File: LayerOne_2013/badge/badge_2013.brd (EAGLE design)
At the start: 81.3 x 81.3 mm, 122 parts, among them CON2 EXT, CON6 J8, CON8 J3, IC4 TL064D, U1 UG-2864HSWEG01, U2 AP7333-33SOT23-3, U4 TPS60403, X2 NX3225GA

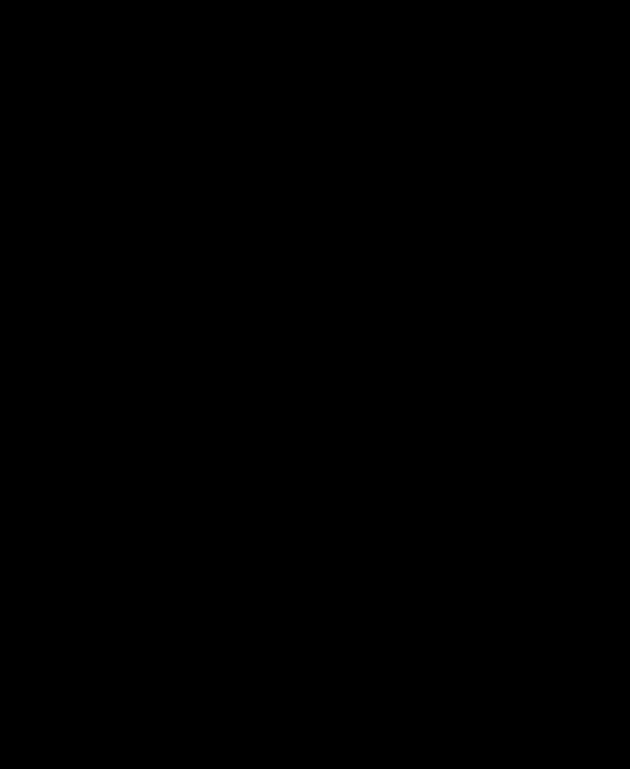
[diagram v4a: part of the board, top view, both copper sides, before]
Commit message: 
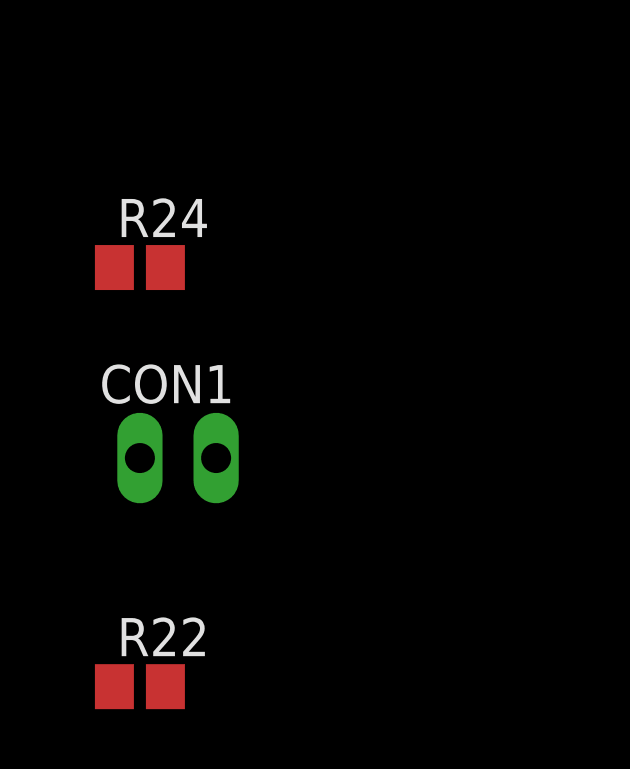
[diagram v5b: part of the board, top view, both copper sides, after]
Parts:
- added CON1: EXT, microbuilder:1X02_OVAL
- added R22: 180K, resistor:R0805
- added R24: 3K, resistor:R0805
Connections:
- removed net RESET: IC2.35
- removed net VBUS: Z1.4
- new net DAC: IC2.6, R22.2
- new net DAT: CON1.1, IC2.34
- new net N$38: CON1.2, IC2.35
- new net N$6: CON2.1, R24.1
- net +5V: now also Z1.4
- net D/C: now also IC2.7; no longer IC2.6
- net N$19: now also R24.2; no longer CON2.1
- net N$24: now also R22.1
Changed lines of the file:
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@@
 <element name="JP1" library="microbuilder" package="JUMPER3" value="" x="16.51" y="3.81"/>
 <element name="SJ1" library="microbuilder" package="SOLDERJUMPER_REFLOW_NOPASTE" value="" x="2.54" y="34.29"/>
+<element name="R24" library="resistor" package="R0805" value="3K" x="-59.69" y="-44.45"/>
+<element name="CON1" library="microbuilder" package="1X02_OVAL" value="EXT" x="-58.42" y="-50.8"/>
+<element name="R22" library="resistor" package="R0805" value="180K" x="-59.69" y="-58.42"/>
 </elements>
 <signals>
@@
 <signal name="N$19">
 <contactref element="IC2" pad="25"/>
-<contactref element="CON2" pad="1"/>
-<wire x1="13.97" y1="-13.97" x2="5.75" y2="-2.4" width="0" layer="19" extent="1-1"/>
+<contactref element="R24" pad="2"/>
+<wire x1="5.75" y1="-2.4" x2="-58.84" y2="-44.45" width="0" layer="19" extent="1-1"/>
 </signal>
 <signal name="+5V">
@@
 <contactref element="IC4" pad="4"/>
 <contactref element="JP6" pad="1"/>
+<contactref element="Z1" pad="4"/>
 <wire x1="-46.09" y1="-10.16" x2="-42.86" y2="-35.29" width="0" layer="19" extent="1-1"/>
 <wire x1="-55.88" y1="1.21" x2="-46.09" y2="-10.16" width="0" layer="19" extent="1-1"/>
@@
 <wire x1="-1.3" y1="13.255" x2="-17.41" y2="24.13" width="0" layer="19" extent="1-16"/>
 <wire x1="22.86" y1="19.05" x2="-1.3" y2="13.255" width="0" layer="19" extent="16-16"/>
-</signal>
-<signal name="VBUS">
-<contactref element="Z1" pad="4"/>
+<wire x1="24.4" y1="0.95" x2="22.86" y2="19.05" width="0" layer="19" extent="16-16"/>
 </signal>
 <signal name="D-">
@@
 <signal name="D/C">
 <contactref element="U1" pad="15"/>
-<contactref element="IC2" pad="6"/>
-<wire x1="-5.75" y1="0" x2="-0.35" y2="26.6" width="0" layer="19" extent="1-1"/>
+<contactref element="IC2" pad="7"/>
+<wire x1="-5.75" y1="-0.8" x2="-0.35" y2="26.6" width="0" layer="19" extent="1-1"/>
 </signal>
 <signal name="R/W">
@@
 <wire x1="-5.75" y1="3.2" x2="-43.6" y2="-6.35" width="0" layer="19" extent="1-1"/>
 </signal>
-<signal name="RESET">
-<contactref element="IC2" pad="35"/>
-</signal>
 <signal name="PA5">
 <contactref element="C4" pad="2"/>
@@
 <contactref element="IC4" pad="13"/>
 <contactref element="C23" pad="1"/>
+<contactref element="R22" pad="1"/>
+<wire x1="-56.78" y1="-17.78" x2="-60.54" y2="-58.42" width="0" layer="19" extent="1-1"/>
 <wire x1="-57.57" y1="-13.97" x2="-56.78" y2="-17.78" width="0" layer="19" extent="1-1"/>
 <wire x1="-58.42" y1="6.41" x2="-57.57" y2="-13.97" width="0" layer="19" extent="1-1"/>
@@
 <wire x1="1.6" y1="5.75" x2="1.44" y2="8.09" width="0" layer="19" extent="1-1"/>
 </signal>
+<signal name="N$6">
+<contactref element="CON2" pad="1"/>
+<contactref element="R24" pad="1"/>
+<wire x1="13.97" y1="-13.97" x2="-60.54" y2="-44.45" width="0" layer="19" extent="1-1"/>
+</signal>
+<signal name="N$38">
+<contactref element="IC2" pad="35"/>
+<contactref element="CON1" pad="2"/>
+<wire x1="3.2" y1="5.75" x2="-57.15" y2="-50.8" width="0" layer="19" extent="1-1"/>
+</signal>
+<signal name="DAT">
+<contactref element="CON1" pad="1"/>
+<contactref element="IC2" pad="34"/>
+<wire x1="4" y1="5.75" x2="-59.69" y2="-50.8" width="0" layer="19" extent="1-1"/>
+</signal>
+<signal name="DAC">
+<contactref element="IC2" pad="6"/>
+<contactref element="R22" pad="2"/>
+<wire x1="-5.75" y1="0" x2="-58.84" y2="-58.42" width="0" layer="19" extent="1-1"/>
+</signal>
 </signals>

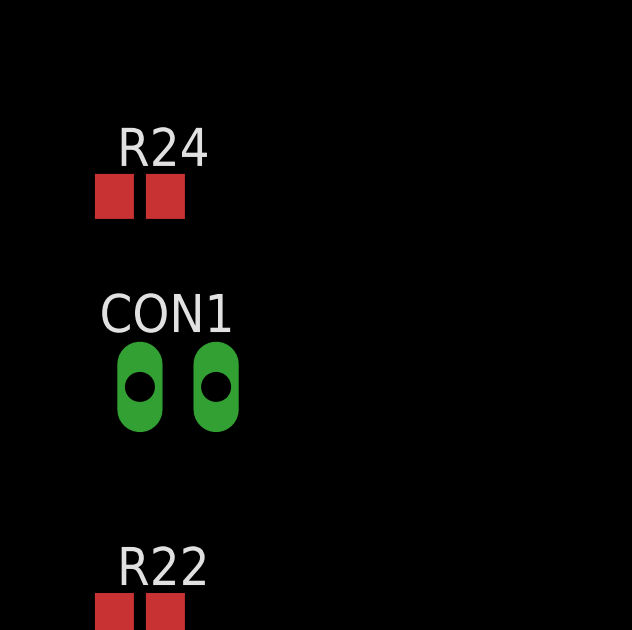
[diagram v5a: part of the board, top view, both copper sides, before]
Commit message: 
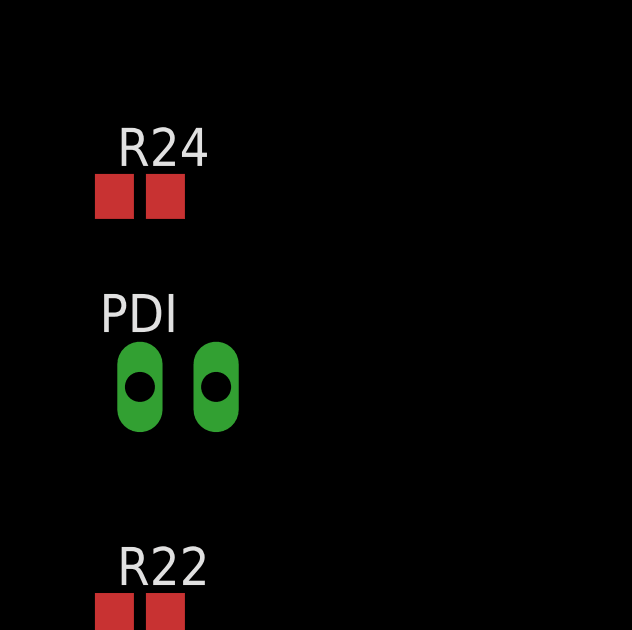
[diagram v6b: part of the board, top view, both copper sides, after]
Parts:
- PDI: value EXT -> CON6
- renumbered CON1 to PDI
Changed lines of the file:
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@@
 <element name="SJ1" library="microbuilder" package="SOLDERJUMPER_REFLOW_NOPASTE" value="" x="2.54" y="34.29"/>
 <element name="R24" library="resistor" package="R0805" value="3K" x="-59.69" y="-44.45"/>
-<element name="CON1" library="microbuilder" package="1X02_OVAL" value="EXT" x="-58.42" y="-50.8"/>
+<element name="PDI" library="microbuilder" package="1X02_OVAL" value="CON6" x="-58.42" y="-50.8"/>
 <element name="R22" library="resistor" package="R0805" value="180K" x="-59.69" y="-58.42"/>
 </elements>
@@
 <signal name="N$38">
 <contactref element="IC2" pad="35"/>
-<contactref element="CON1" pad="2"/>
+<contactref element="PDI" pad="2"/>
 <wire x1="3.2" y1="5.75" x2="-57.15" y2="-50.8" width="0" layer="19" extent="1-1"/>
 </signal>
 <signal name="DAT">
-<contactref element="CON1" pad="1"/>
+<contactref element="PDI" pad="1"/>
 <contactref element="IC2" pad="34"/>
 <wire x1="4" y1="5.75" x2="-59.69" y2="-50.8" width="0" layer="19" extent="1-1"/>

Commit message: 
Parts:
- C10, C11: value 0.1uF -> 10pF
- C16: value 330pF -> 4.7pF
- C25: value 1uF -> 4.7uF
- C4: value 0.1uF -> 330pF
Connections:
- removed net N$15: C12.1, IC2.39
- net +3.3V: now also C12.1, IC2.39
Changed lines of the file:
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@@
 <element name="C1" library="SparkFun" package="0805" value="1uF" x="3.81" y="-20.32" rot="R90"/>
 <element name="C3" library="SparkFun" package="0805" value="1uF" x="-16.51" y="24.13"/>
-<element name="C4" library="SparkFun" package="0805" value="0.1uF" x="-11.43" y="5.08"/>
+<element name="C4" library="SparkFun" package="0805" value="330pF" x="-11.43" y="5.08"/>
 <element name="JP2" library="microbuilder" package="1X02_OVAL" value="" x="7.62" y="-20.32" rot="R270"/>
 <element name="CH1" library="microbuilder" package="1X02_OVAL" value="CON2" x="-22.86" y="-13.97"/>
@@
 <element name="R4" library="resistor" package="R0805" value="3K" x="-44.45" y="-15.24"/>
 <element name="C2" library="SparkFun" package="0805" value="330pF" x="-50.8" y="-8.89"/>
-<element name="C16" library="SparkFun" package="0805" value="330pF" x="-46.99" y="-10.16"/>
+<element name="C16" library="SparkFun" package="0805" value="4.7pF" x="-46.99" y="-10.16"/>
 <element name="CH2" library="microbuilder" package="1X02_OVAL" value="CON2" x="-16.51" y="-13.97"/>
 <element name="R10" library="resistor" package="R0805" value="820K" x="-55.88" y="-21.59"/>
@@
 <element name="R6" library="resistor" package="R0805" value="3K" x="-45.72" y="21.59"/>
 <element name="U4" library="RHD2000_eval_board" package="SOT-23-5" value="TPS60403" x="-46.99" y="16.51"/>
-<element name="C25" library="SparkFun" package="0805" value="1uF" x="-58.42" y="19.05"/>
+<element name="C25" library="SparkFun" package="0805" value="4.7uF" x="-58.42" y="19.05"/>
 <element name="C24" library="SparkFun" package="0805" value="0.1uF" x="-58.42" y="21.59"/>
 <element name="C26" library="SparkFun" package="0805" value="0.1uF" x="-58.42" y="24.13"/>
@@
 <element name="C23" library="SparkFun" package="0805" value="10pF" x="-55.88" y="-17.78"/>
 <element name="X2" library="M6-RF315" package="NX3225GA" value="NX3225GA" x="2.54" y="8.89"/>
-<element name="C10" library="SparkFun" package="0805" value="0.1uF" x="-1.27" y="8.89" rot="R270"/>
-<element name="C11" library="SparkFun" package="0805" value="0.1uF" x="6.35" y="8.89" rot="R90"/>
+<element name="C10" library="SparkFun" package="0805" value="10pF" x="-1.27" y="8.89" rot="R270"/>
+<element name="C11" library="SparkFun" package="0805" value="10pF" x="6.35" y="8.89" rot="R90"/>
 <element name="K1" library="switch-omron" package="B3F-5XX" value="" x="-15.24" y="-25.4" rot="R90"/>
 <element name="K2" library="switch-omron" package="B3F-5XX" value="" x="-5.08" y="-29.21" rot="R90"/>
@@
 <contactref element="LED48" pad="A"/>
 <contactref element="LED26" pad="A"/>
+<contactref element="IC2" pad="39"/>
+<contactref element="C12" pad="1"/>
 <wire x1="-30.999125" y1="-22.18518125" x2="-37.73" y2="-25.4" width="0" layer="19" extent="1-1"/>
 <wire x1="-33.6296" y1="-17.950146875" x2="-30.999125" y2="-22.18518125" width="0" layer="19" extent="1-1"/>
@@
 <wire x1="29.452871875" y1="-24.200296875" x2="32.3596" y2="-20.14985" width="0" layer="19" extent="1-1"/>
 <wire x1="26.043753125" y1="-27.83980625" x2="22.18518125" y2="-30.999125" width="0" layer="19" extent="1-1"/>
+<wire x1="22.86" y1="-8.52" x2="32.65" y2="-8.89" width="0" layer="19" extent="1-1"/>
 <wire x1="-6.65" y1="26.6" x2="-8.633553125" y2="37.130759375" width="0" layer="19" extent="1-1"/>
 <wire x1="-4.55" y1="26.6" x2="-6.65" y2="26.6" width="0" layer="19" extent="1-1"/>
-<wire x1="23.065" y1="3.95" x2="32.65" y2="-6.35" width="0" layer="19" extent="1-1"/>
+<wire x1="23.065" y1="3.95" x2="22.86" y2="-8.52" width="0" layer="19" extent="1-1"/>
 <wire x1="16.51" y1="3.81" x2="23.065" y2="3.95" width="0" layer="19" extent="1-1"/>
 <wire x1="5.75" y1="2.4" x2="16.51" y2="3.81" width="0" layer="19" extent="1-1"/>
+<wire x1="0" y1="5.75" x2="5.75" y2="2.4" width="0" layer="19" extent="1-1"/>
 <wire x1="1.6" y1="-5.75" x2="5.75" y2="2.4" width="0" layer="19" extent="1-1"/>
 <wire x1="-5.75" y1="-2.4" x2="1.6" y2="-5.75" width="0" layer="19" extent="1-1"/>
@@
 <wire x1="5.75" y1="-3.2" x2="-17.78" y2="-4.86" width="0" layer="19" extent="1-1"/>
 </signal>
-<signal name="N$15">
-<contactref element="IC2" pad="39"/>
-<contactref element="C12" pad="1"/>
-<wire x1="0" y1="5.75" x2="22.86" y2="-8.52" width="0" layer="19" extent="1-1"/>
-</signal>
 <signal name="COL2">

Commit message: oled update
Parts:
- SJ1: device microbuilder:SOLDERJUMPER_REFLOW_NOPASTE -> microbuilder:SOLDERJUMPER_REFLOW
- U1: device microbuilder:UG-2864HSWEG01_0.96IN_WRAPAROUND -> badge.lbrbadge_2013:MICROBUILDER_UG-2864HSWEG01_0.96IN_WRAPAROUND
- moved IC4 45.1 mm to (-11.4, -3.81), turned to 180 degrees
- moved JP6 28.1 mm to (-27.9, 15.2)
- moved R22 24.7 mm to (-39.4, -44.5)
- moved SJ1 22.5 mm to (-3.81, 12.7), turned to 180 degrees
- moved R24 13.1 mm to (-66.0, -33.0)
- moved PDI 11.4 mm to (-58.4, -39.4)
- moved D3 9.67 mm to (-26.7, -7.62)
- moved D2 9.25 mm to (-21.6, -6.35)
- moved IC2 8.52 mm to (7.62, -3.81)
- moved U1 6.35 mm to (0.00, 19.1), turned to 0 degrees
- moved C10 5.68 mm to (3.81, 6.35)
- moved C11 5.68 mm to (11.4, 6.35)
- moved X2 5.68 mm to (7.62, 6.35)
- moved JP1 3.59 mm to (19.1, 6.35)
- moved D1 1.27 mm to (-16.5, 12.7)
